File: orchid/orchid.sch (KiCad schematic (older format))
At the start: 117 parts, among them J1 NEIGHBOR1, J2 NEIGHBOR2, J7 BONUS_ROW, U1 ADF7242, U2 ADF7242, U3 ADF7242, U4 ADF7242

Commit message: Working on Orchid pcb layout
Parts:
- added C12, C39, C42, C9: 200nF, gsg-modules:0402, symbol C
- added C15, C18, C45, C48: 27pF, gsg-modules:0402, symbol C
- added J10, J11, J12, J13, J14, J15, J16, J19, J20, J21, J22, J23, J24, J25, J26, J9: TEST_2P, gsg-modules:0603-JUMPER, symbol TEST_2P
- added J27, J28, J8: Conn_01x04, gsg-modules:HEADER-1x4, symbol Conn_01x04
- C1, C10, C11, C13, C14, C16, C17, C19, C2, C20, C21, C22, C23, C24, C25, C26, C27, C28, C29, C3, C30, C31, C32, C33, C34, C35, C36, C37, C38, C4, C40, C41, C43, C44, C46, C47, C49, C5, C50, C51, C52, C53, C54, C55, C56, C57, C58, C59, C6, C60, C61, C62, C63, C64, C65, C66, C67, C68, C69, C7, C70, C71, C72, C73, C74, C75, C76, C77, C78, C79, C8, C80: renamed from C?; footprint (none) -> gsg-modules:0402
- J17, J18: renamed from J?; footprint (none) -> gsg-modules:SMA-EDGE
- J3, J4, J5, J6: renamed from J?; footprint (none) -> gsg-modules:HEADER-1x6
- L1, L10, L11, L12, L13, L14, L15, L2, L3, L4, L5, L6, L7, L8, L9: renamed from L?; footprint (none) -> gsg-modules:0402
- R1, R2, R3, R4, R5, R6, R7, R8: renamed from R?; footprint (none) -> gsg-modules:0402
- U1, U2, U3, U4: footprint (none) -> gsg-modules:LFCSP32
- U5: renamed from U?; footprint (none) -> gsg-modules:SKY13322-375LF
- X1, X2, X3, X4: renamed from X?; footprint (none) -> gsg-modules:XTAL3.2x2.5mm
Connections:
- net labels added: IRQ1, IRQ2, IRQ3, IRQ4, TRFS1, TRFS2, TRFS3, TRFS4
- wire segments 452 -> 547
- no-connect marks 0 -> 66
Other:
- note added: "SPI/SPORT connections"
- note added: "default pin\nalt pin"
- moved on the sheet: J7

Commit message: Completed PCB layout
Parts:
- J3, J4, J5, J6: footprint gsg-modules:HEADER-1x6 -> gsg-modules:HEADER-2x3
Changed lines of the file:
@@
 Text Label 15300 5900 0    40   ~ 0
 P9_5
-Text Label 15300 6100 0    40   ~ 0
-P1_20
 Text Label 16200 5900 2    40   ~ 0
 P9_6
@@
 F 0 "J5" H 8300 1200 50  0000 C CNN
 F 1 "Conn_01x06" H 8300 500 50  0000 C CNN
-F 2 "gsg-modules:HEADER-1x6" H 8300 900 50  0001 C CNN
+F 2 "gsg-modules:HEADER-2x3" H 8300 900 50  0001 C CNN
 F 3 "" H 8300 900 50  0001 C CNN
 	1    8300 900
@@
 F 0 "J3" H 3900 1250 50  0000 C CNN
 F 1 "Conn_01x06" H 3900 550 50  0000 C CNN
-F 2 "gsg-modules:HEADER-1x6" H 3900 950 50  0001 C CNN
+F 2 "gsg-modules:HEADER-2x3" H 3900 950 50  0001 C CNN
 F 3 "" H 3900 950 50  0001 C CNN
 	1    3900 950
@@
 F 0 "J4" H 3950 6100 50  0000 C CNN
 F 1 "Conn_01x06" H 3950 5400 50  0000 C CNN
-F 2 "gsg-modules:HEADER-1x6" H 3950 5800 50  0001 C CNN
+F 2 "gsg-modules:HEADER-2x3" H 3950 5800 50  0001 C CNN
 F 3 "" H 3950 5800 50  0001 C CNN
 	1    3950 5800
@@
 F 0 "J6" H 8400 6100 50  0000 C CNN
 F 1 "Conn_01x06" H 8400 5400 50  0000 C CNN
-F 2 "gsg-modules:HEADER-1x6" H 8400 5800 50  0001 C CNN
+F 2 "gsg-modules:HEADER-2x3" H 8400 5800 50  0001 C CNN
 F 3 "" H 8400 5800 50  0001 C CNN
 	1    8400 5800
@@
 P6_3
 Text Label 10500 9200 0    60   ~ 0
-P6_6
+P1_0
 Text Label 10500 9600 0    60   ~ 0
 P2_2
 Text Label 10500 10000 0    60   ~ 0
-P6_8
+P1_16
 Text Label 10500 9000 0    60   ~ 0
-P1_15
+P2_5
 Text Label 10500 9400 0    60   ~ 0
-P9_5
+P1_5
 Text Label 10500 9800 0    60   ~ 0
-P1_18
+P6_8
 $Comp
 L Conn_01x04 J8
@@
 	9400 8650 9250 8650
 Text Label 12800 7250 0    60   ~ 0
-P1_20
+P4_3
 Text Label 10500 10200 0    60   ~ 0
-P1_6
+P1_20
 Text Label 12800 7650 0    60   ~ 0
-P6_0
+P5_2
 Text Label 12800 8050 0    60   ~ 0
-P2_0
+P3_5
 Text Label 12800 8450 0    60   ~ 0
 P9_6
 Text Label 12800 7450 0    60   ~ 0
-P6_7
+P4_4
 Text Label 12800 7850 0    60   ~ 0
-P3_7
+P1_6
 Text Label 12800 8250 0    60   ~ 0
 P3_4
 Text Label 12800 8650 0    60   ~ 0
-P2_3
+P9_5
 $Comp
 L SKY13322 U5
@@
 NoConn ~ 15300 2050
 NoConn ~ 15250 2150
-NoConn ~ 15300 2250
-NoConn ~ 15300 2350
 NoConn ~ 16000 1950
 NoConn ~ 16200 2050
@@
 NoConn ~ 15300 2950
 NoConn ~ 15300 3650
-NoConn ~ 15300 3750
 NoConn ~ 15200 3850
 NoConn ~ 16300 3850
@@
 NoConn ~ 16200 3050
 NoConn ~ 16200 2950
-NoConn ~ 16200 2750
 NoConn ~ 16200 2650
 NoConn ~ 16200 2550
@@
 NoConn ~ 15300 4400
 NoConn ~ 15300 4500
-NoConn ~ 15300 4600
 NoConn ~ 15300 4700
 NoConn ~ 15300 4800
-NoConn ~ 15300 4900
 NoConn ~ 15300 5000
 NoConn ~ 15300 5100
@@
 NoConn ~ 15300 5600
 NoConn ~ 15300 5700
-NoConn ~ 16200 5700
 NoConn ~ 16200 5400
 NoConn ~ 16200 5300
 NoConn ~ 16200 5200
 NoConn ~ 16200 5100
-NoConn ~ 16200 4900
 NoConn ~ 16200 4800
 NoConn ~ 16200 4700
@@
 NoConn ~ 15850 7550
 NoConn ~ 15950 7550
+NoConn ~ 15300 3450
+Text Label 15300 6100 0    40   ~ 0
+P1_20
+NoConn ~ 16200 6000
+NoConn ~ 16200 3350
+NoConn ~ 16200 3550
+NoConn ~ 16200 2850
+NoConn ~ 16200 5600
+NoConn ~ 15300 6000
+NoConn ~ 15300 5800
 $EndSCHEMATC

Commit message: Added silkscreen labels for headers
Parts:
- C1, C2, C31, C32, C36, C38, C6, C8: Description (none) -> CAP CER 100PF 25V X7R 0402; Manufacturer (none) -> Wurth Electronics Inc.; Part Number (none) -> 732-7533-1-ND
- C10, C11, C13, C14, C24, C26, C3, C33, C34, C4, C40, C41, C43, C44, C54, C56: Description (none) -> CAP CER 0.22UF 10V X5R 0402; Manufacturer (none) -> Wurth Electronics Inc.; Part Number (none) -> 732-7488-1-ND
- C12, C39, C42, C9: value 200nF -> 220nF; Description (none) -> CAP CER 0.22UF 10V X5R 0402; Manufacturer (none) -> Wurth Electronics Inc.; Part Number (none) -> 732-7488-1-ND
- C15, C16, C17, C18, C19, C20, C27, C29, C35, C37, C45, C46, C47, C48, C49, C5, C50, C57, C59, C7: Description (none) -> CAP CER 27PF 50V C0G/NP0 0402; Manufacturer (none) -> KEMET; Part Number (none) -> 399-8960-1-ND
- C21, C22, C28, C30, C51, C52, C58, C60: Description (none) -> CAP CER 18PF 50V C0G/NP0 0402; Manufacturer (none) -> KEMET; Part Number (none) -> 399-8952-1-ND
- C23, C25, C53, C55: Description (none) -> CAP CER 1000PF 10V X7R 0402; Manufacturer (none) -> Wurth Electronics Inc.; Part Number (none) -> 732-7501-1-ND
- C61, C62, C63, C64, C65, C66, C73, C74, C75, C76: Description (none) -> CAP CER 1PF 25V C0G/NP0 0402; Manufacturer (none) -> Wurth Electronics Inc.; Part Number (none) -> 732-7450-1-ND
- C67, C68, C69, C70, C71, C72, C77, C78, C79, C80: Description (none) -> CAP CER 10000PF 10V X7R 0402; Manufacturer (none) -> Wurth Electronics Inc.; Part Number (none) -> 732-7507-1-ND
- J10, J11, J12, J13, J14, J15, J16, J19, J20, J21, J22, J23, J24, J25, J26, J9: Note (none) -> DNP
- J17, J18: Description (none) -> CONN RPSMA RCPT STR 50OHM EDGEMT; Manufacturer (none) -> Linx Technologies Inc.; Part Number (none) -> CONREVSMA003.062-ND
- J27, J28, J8: Description (none) -> CONN RECEPT 2MM SINGLE STR 4POS; Manufacturer (none) -> Sullins Connector Solutions; Part Number (none) -> S5751-04-ND
- J3, J4, J5, J6: Description (none) -> CONN RECEPT 2MM DUAL STR 6POS; Manufacturer (none) -> Sullins Connector Solutions; Part Number (none) -> S5750-03-ND
- L1, L10, L11, L12, L14, L2, L3, L4, L6, L8: Description (none) -> FIXED IND 2.7NH 300MA 170 MOHM; Manufacturer (none) -> Samsung Electro-Mechanics; Part Number (none) -> 1276-6292-1-ND
- L13, L15, L5, L7, L9: Description (none) -> FIXED IND 9.5NH 540MA 140 MOHM; Manufacturer (none) -> Murata Electronics North America; Part Number (none) -> 490-8445-1-ND
- R1, R2, R5, R6: Description (none) -> RES 27K OHM 5% 1/16W 0402; Manufacturer (none) -> Stackpole Electronics Inc.; Part Number (none) -> RMCF0402JT27K0CT-ND
- R3, R4, R7, R8: Description (none) -> RES 10K OHM 5% 1/16W 0402; Manufacturer (none) -> Stackpole Electronics Inc.; Part Number (none) -> RMCF0402JT10K0CT-ND
- U1, U2, U3, U4: Description (none) -> IC RF TXRX+MCU 802.15.4 32-WFQFN; Manufacturer (none) -> Analog Devices Inc.; Part Number (none) -> ADF7242BCPZ-ND
- U5: Description (none) -> IC SWITCH SP4T 0.1-6GHZ 10MLPD; Manufacturer (none) -> Skyworks Solutions Inc.; Part Number (none) -> 863-1176-1-ND
- X1, X2, X3, X4: Description (none) -> CRYSTAL 26.0000MHZ 10PF SMD; Manufacturer (none) -> NDK America, Inc.; Part Number (none) -> 644-1101-1-ND

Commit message: Revised Lucky Bamboo schematic and PCB layout: Added LNA amplifiers on RF input stage and baluns for all RF input/output ports. Added connections from IRQ1/IRQ2 to GreatFET header. Updated GSG Kicad library.
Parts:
- removed J27, J28, J8: Conn_01x04, gsg-modules:HEADER-1x4, symbol Conn_01x04
- removed J3, J4, J5, J6: Conn_01x06, gsg-modules:HEADER-2x3, symbol Conn_01x06
- removed L10, L11, L12, L14, L2, L3, L4, L6, L8: 2n7, gsg-modules:0402, symbol L
- removed L13, L15, L5, L7, L9: 9n5, gsg-modules:0402, symbol L
- added C81: 10nF, gsg-modules:0402, symbol C
- added J27, J28, J29, J30, J31, J32, J33, J8: TEST_2P, gsg-modules:0603-JUMPER, symbol TEST_2P
- added J3, J4, J5, J6: Conn_01x08, gsg-modules:HEADER-2x4, symbol Conn_01x08
- added U10, U11, U14, U15, U16, U17, U8, U9: ADF7242_balun, gsg-modules:ADF7242_balun, symbol ADF7242_balun
- added U12, U13, U6, U7: BGA7H1N6, gsg-modules:TSNP-6-2, symbol BGA7H1N6
- C61, C62, C63, C66: value 1pF -> 1nF; Description CAP CER 1PF 25V C0G/NP0 0402 -> CAP CER 1000PF 10V X7R 0402; Part Number 732-7450-1-ND -> 732-7501-1-ND
- C64, C65, C73, C74, C75, C76: value 1pF -> 10nF; Description CAP CER 1PF 25V C0G/NP0 0402 -> CAP CER 10000PF 10V X7R 0402; Part Number 732-7450-1-ND -> 732-7507-1-ND
- C67: value 10nF -> 1nF; Description CAP CER 10000PF 10V X7R 0402 -> CAP CER 1000PF 10V X7R 0402; Part Number 732-7507-1-ND -> 732-7501-1-ND
- L1: value 2n7 -> 3.8nH; Description FIXED IND 2.7NH 300MA 170 MOHM -> FIXED IND 3.8NH 340MA 550 MOHM; Manufacturer Samsung Electro-Mechanics -> Abracon LLC; Part Number 1276-6292-1-ND -> 535-10379-1-ND
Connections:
- net labels added: PABIAOP1, PABIAOP2, PABIAOP3, PABIAOP4, PAVSUP1, PAVSUP2, PAVSUP3, PAVSUP4, RFIN, RFIN1, RFIN1_N, RFIN1_P, RFIN2, RFIN2_N, RFIN2_P, RFIN3, RFIN3_N, RFIN3_P, RFIN4, RFIN4_N, RFIN4_P, RXEN1, RXEN2, RXEN3, RXEN4, TXEN1, TXEN2, TXEN3, TXEN4, XOSC32KN1, XOSC32KN2, XOSC32KN3, XOSC32KN4, XOSC32KP1, XOSC32KP2, XOSC32KP3, XOSC32KP4
- net labels removed: RFIN_N, RFIN_P
- wire segments 547 -> 444
- no-connect marks 66 -> 58
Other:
- note added: "RF input"
- note added: "RF input amplifiers"
- note added: "RF input baluns"
- note removed: "RF input balun"
- moved on the sheet: C1, C10, C11, C12, C13, C14, C15, C16, C17, C18, C19, C2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

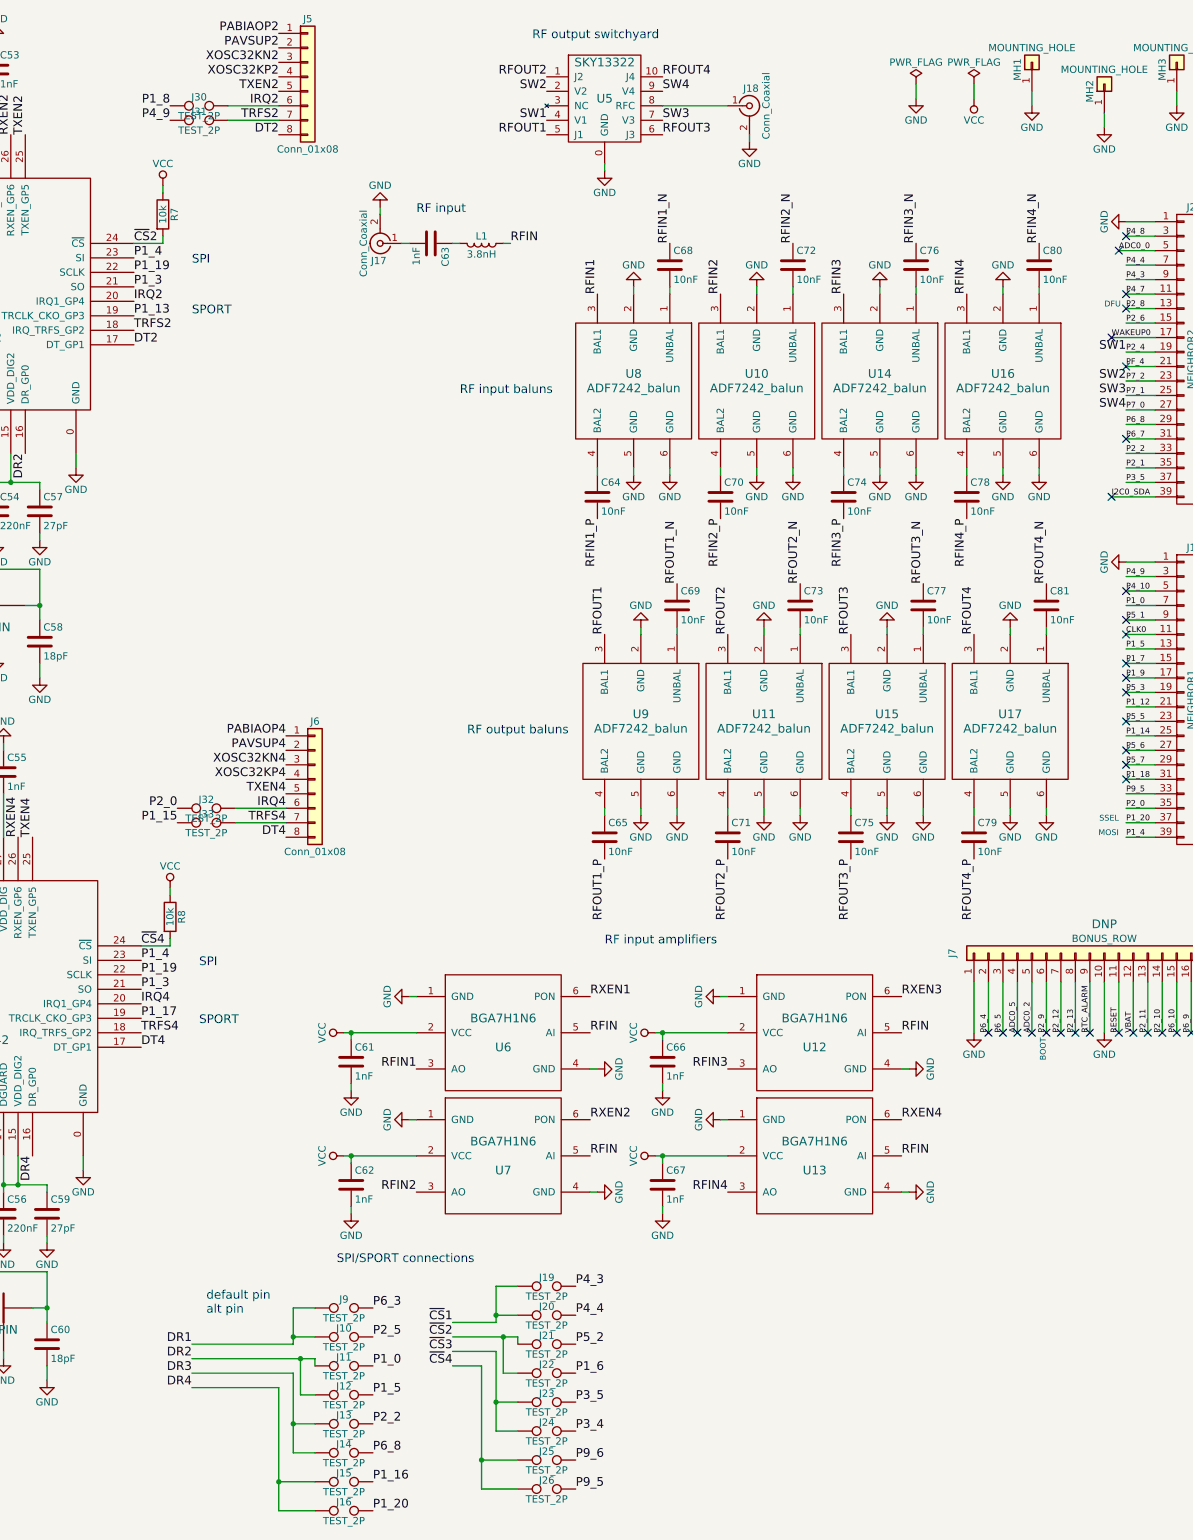
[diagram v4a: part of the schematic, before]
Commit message: Corrected Lily BOM. Updated gsg-kicad-lib
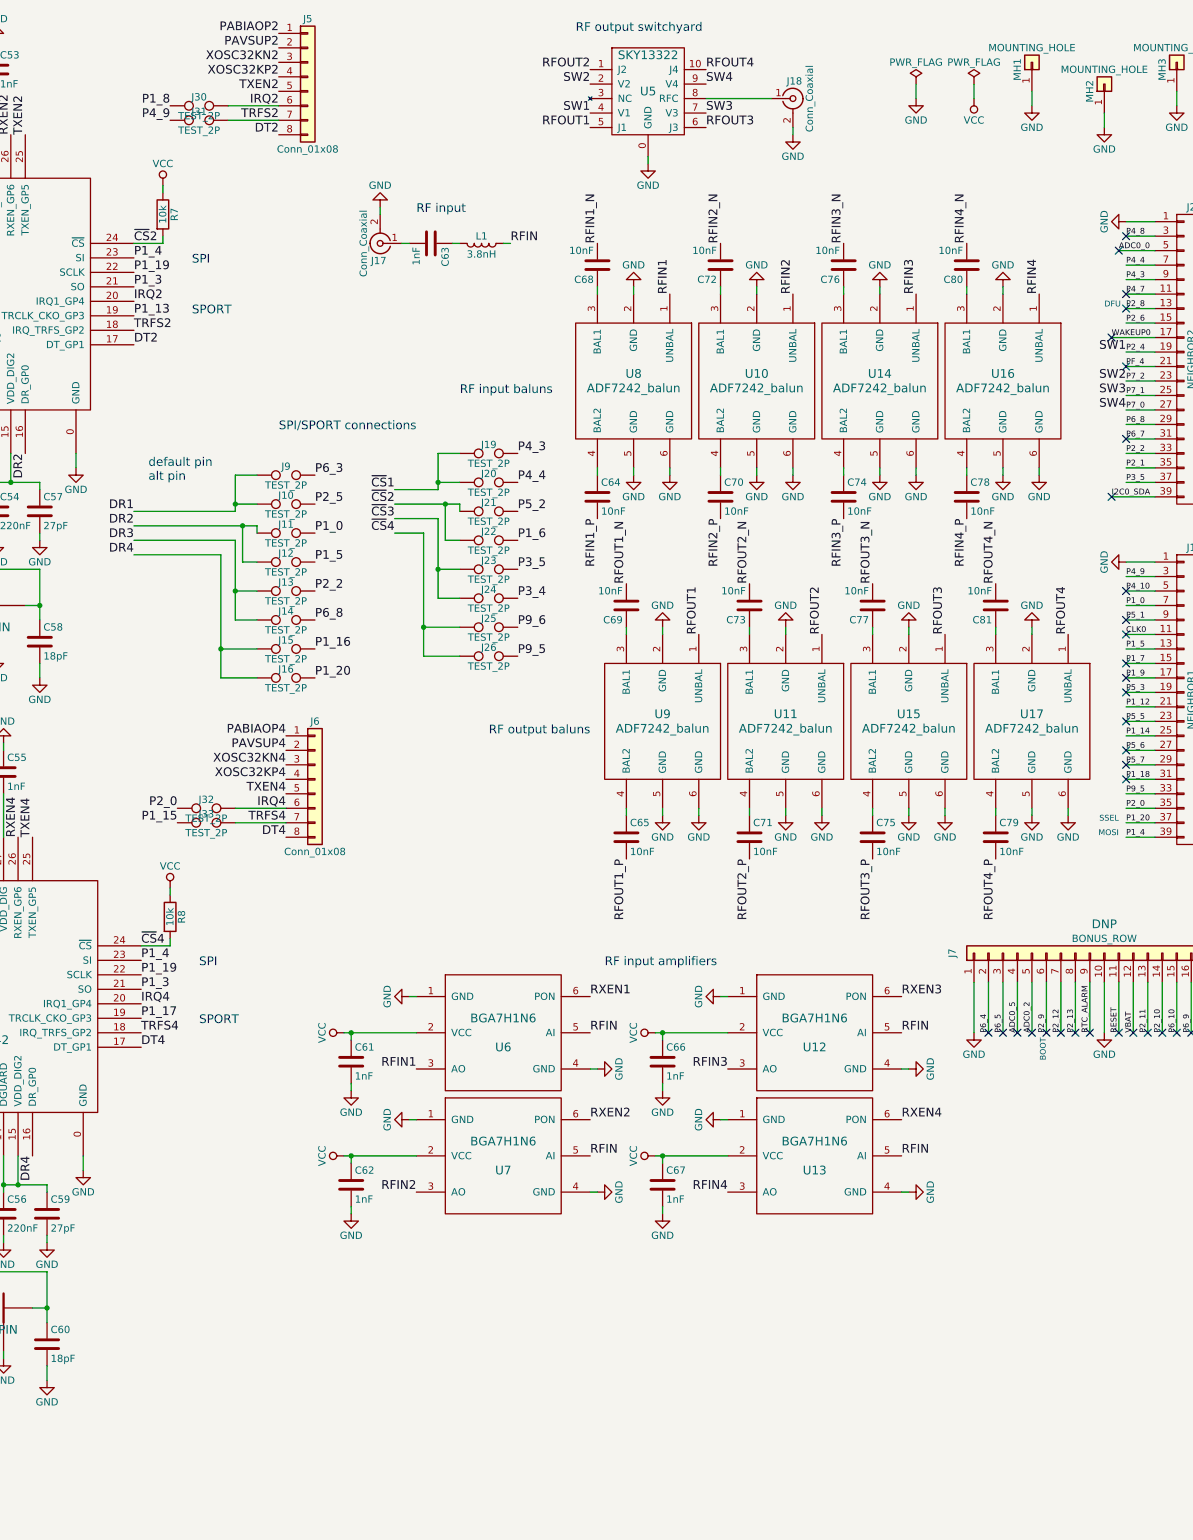
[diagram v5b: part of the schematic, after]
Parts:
- C1, C2, C31, C32, C36, C38, C6, C8: Part Number 732-7533-1-ND -> 885012205038
- C10, C11, C12, C13, C14, C24, C26, C3, C33, C34, C39, C4, C40, C41, C42, C43, C44, C54, C56, C9: Part Number 732-7488-1-ND -> 885012105011
- C15, C16, C17, C18, C19, C20, C27, C29, C35, C37, C45, C46, C47, C48, C49, C5, C50, C57, C59, C7: Part Number 399-8960-1-ND -> C0402C270K5GACTU
- C21, C22, C28, C30, C51, C52, C58, C60: Part Number 399-8952-1-ND -> C0402C180J5GAC7867
- C23, C25, C53, C55, C61, C62, C63, C66, C67: Part Number 732-7501-1-ND -> 885012205006
- C64, C65, C68, C69, C70, C71, C72, C73, C74, C75, C76, C77, C78, C79, C80, C81: Part Number 732-7507-1-ND -> 885012205012
- J17, J18: Description CONN RPSMA RCPT STR 50OHM EDGEMT -> CONN SMA RCPT STR 50OHM EDGE MNT; Part Number CONREVSMA003.062-ND -> CONSMA003.062
- J3, J4, J5, J6: Part Number S5750-04-ND -> NPPN042AFCN-RC
- L1: Part Number 535-10379-1-ND -> ATFC-0402-3N8B-T
- R1, R2, R5, R6: Part Number RMCF0402JT27K0CT-ND -> RMCF0402JT27K0
- R3, R4, R7, R8: Part Number RMCF0402JT10K0CT-ND -> RMCF0402JT10K0
- U1, U2, U3, U4: Part Number ADF7242BCPZ-ND -> ADF7242BCPZ
- U10, U11, U14, U15, U16, U17, U8, U9: Part Number 712-1575-1-ND -> 2450BM14E0007T
- U12, U13, U6, U7: Part Number BGA7H1N6E6327XTSA1CT-ND -> BGA7H1N6E6327XTSA1
- U5: Part Number 863-1176-1-ND -> SKY13322-375LF
- X1, X2, X3, X4: Part Number 644-1101-1-ND -> NX3225SA-26.000000MHZ-B1
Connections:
- net RFIN1: now also U8.1 (UNBAL); no longer U8.3 (BAL1)
- net RFIN1_N: now also C68.2; no longer C68.1
- net RFIN2: now also U10.1 (UNBAL); no longer U10.3 (BAL1)
- net RFIN2_N: now also C72.2; no longer C72.1
- net RFIN3: now also U14.1 (UNBAL); no longer U14.3 (BAL1)
- net RFIN3_N: now also C76.2; no longer C76.1
- net RFIN4: now also U16.1 (UNBAL); no longer U16.3 (BAL1)
- net RFIN4_N: now also C80.2; no longer C80.1
- net RFOUT1: now also U9.1 (UNBAL); no longer U9.3 (BAL1)
- net RFOUT1_N: now also C69.2; no longer C69.1
- net RFOUT2: now also U11.1 (UNBAL); no longer U11.3 (BAL1)
- net RFOUT2_N: now also C73.2; no longer C73.1
- net RFOUT3: now also U15.1 (UNBAL); no longer U15.3 (BAL1)
- net RFOUT3_N: now also C77.2; no longer C77.1
- net RFOUT4: now also U17.1 (UNBAL); no longer U17.3 (BAL1)
- net RFOUT4_N: now also C81.2; no longer C81.1
- new net: C69.1, U9.3 (BAL1)
- new net: C73.1, U11.3 (BAL1)
- new net: C77.1, U15.3 (BAL1)
- new net: C81.1, U17.3 (BAL1)
- new net: C68.1, U8.3 (BAL1)
- new net: C72.1, U10.3 (BAL1)
- new net: C76.1, U14.3 (BAL1)
- new net: C80.1, U16.3 (BAL1)
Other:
- moved on the sheet: C65, C68, C69, C71, C72, C73, C75, C76, C77, C79, C80, C81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

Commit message: Added RF splitter/amp to orchid schematic
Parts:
- removed C61, C62, C66, C67: 1nF, gsg-modules:0402, symbol C
- removed U12, U13, U6, U7: BGA7H1N6, gsg-modules:TSNP-6-2, symbol BGA7H1N6
- added C?: 1nF, gsg-modules:0402, symbol RF_divider_test-rescue:C
- added R? (x3): 100, gsg-modules:0603, symbol RF_divider_test-rescue:R
- added U? (x3): HHM2293A1, gsg-modules:HHM2293A1, symbol RF_divider_test-rescue:HHM2293A1
- added U?: BGA7H1N6, gsg-modules:TSNP-6-2, symbol RF_divider_test-rescue:BGA7H1N6
- C1, C10, C11, C12, C13, C14, C15, C16, C17, C18, C19, C2, C20, C21, C22, C23, C24, C25, C26, C27, C28, C29, C3, C30, C31, C32, C33, C34, C35, C36, C37, C38, C39, C4, C40, C41, C42, C43, C44, C45, C46, C47, C48, C49, C5, C50, C51, C52, C53, C54, C55, C56, C57, C58, C59, C6, C60, C63, C64, C65, C68, C69, C7, C70, C71, C72, C73, C74, C75, C76, C77, C78, C79, C8, C80, C81, C9: symbol C -> orchid-rescue:C
- J1, J2: symbol CONN_02X20 -> orchid-rescue:CONN_02X20
- J10, J11, J12, J13, J14, J15, J16, J19, J20, J21, J22, J23, J24, J25, J26, J27, J28, J29, J30, J31, J32, J33, J8, J9: symbol TEST_2P -> orchid-rescue:TEST_2P
- J17, J18: symbol Conn_Coaxial -> orchid-rescue:Conn_Coaxial
- J3, J4, J5, J6: symbol Conn_01x08 -> orchid-rescue:Conn_01x08
- J7: symbol Conn_01x20 -> orchid-rescue:Conn_01x20
- L1: symbol L -> orchid-rescue:L
- MH1, MH2, MH3, MH4: symbol Conn_01x01 -> orchid-rescue:Conn_01x01
- R1, R2, R3, R4, R5, R6, R7, R8: symbol R -> orchid-rescue:R
- U1, U2, U3, U4: symbol ADF7242 -> orchid-rescue:ADF7242
- U10, U11, U14, U15, U16, U17, U8, U9: symbol ADF7242_balun -> orchid-rescue:ADF7242_balun
- U5: symbol SKY13322 -> orchid-rescue:SKY13322
- X1, X2, X3, X4: symbol XTAL4PIN -> orchid-rescue:XTAL4PIN
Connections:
- wire segments 444 -> 511
- no-connect marks 58 -> 57
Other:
- note added: "RX Amplifier/Splitter"
- note added: "RX_AMP"
- note added: "Toggle J1 \npin 5\n(GPIO5[14])\nto turn\non/off amp"
- note removed: "RF input amplifiers"
